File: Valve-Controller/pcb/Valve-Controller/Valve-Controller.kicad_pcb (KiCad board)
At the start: 2 copper layers, 26.9 x 26.9 mm, 14 parts, among them J1 Screw_Terminal_01x02, J2 Conn_01x03_Socket, Q1 SiS454DN

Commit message: Updated Valve Controller PCB and BOM
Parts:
- added D1: D, Diode_SMD:D_SOD-123, F.Cu at (40.8, 32.1)
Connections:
- net +3.3V renamed +12V
- net /PyroController/Input renamed /ValveController/Input
- net /PyroController/Output renamed /ValveController/Output
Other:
- board text added: "Valve Controller Rev. 1"
- board text removed: "Pyro Controller Rev. 1"

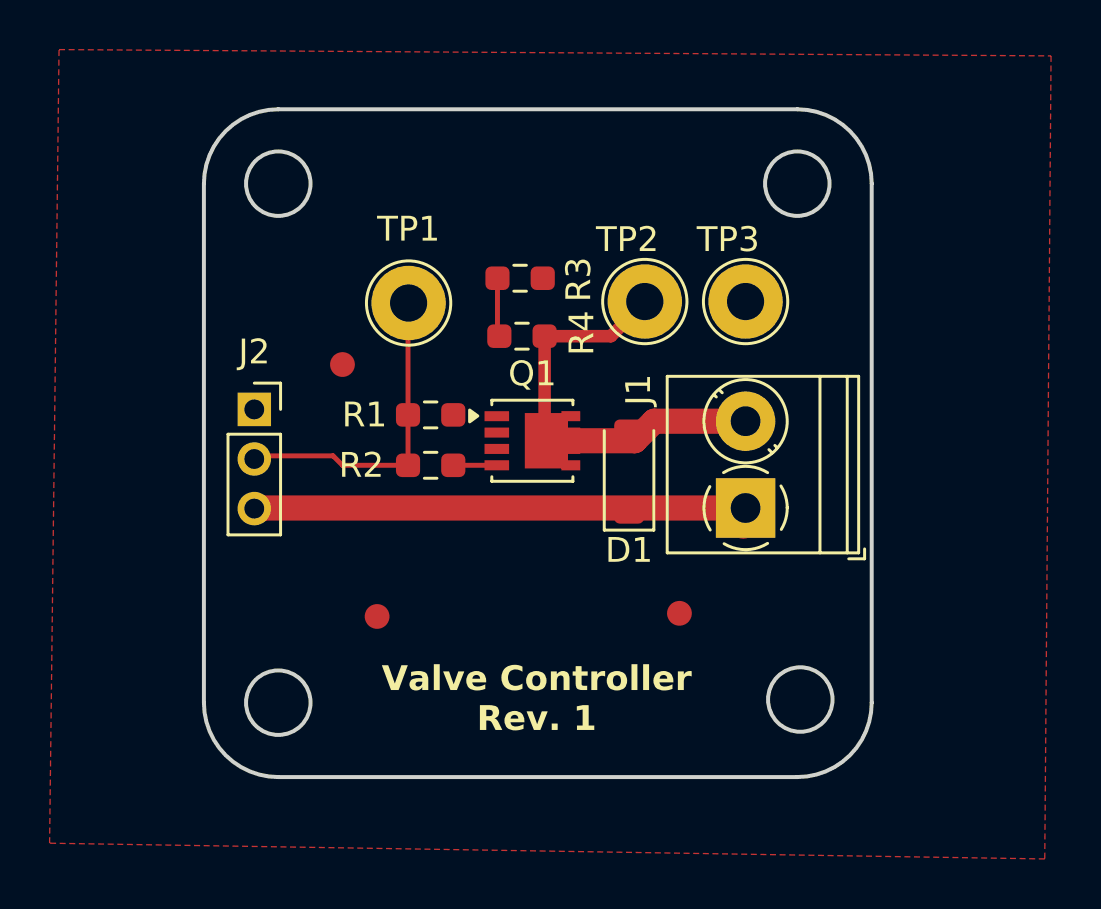
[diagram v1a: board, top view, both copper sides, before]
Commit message: Fixed valve controller pin socket. Now 2.54mm pitch
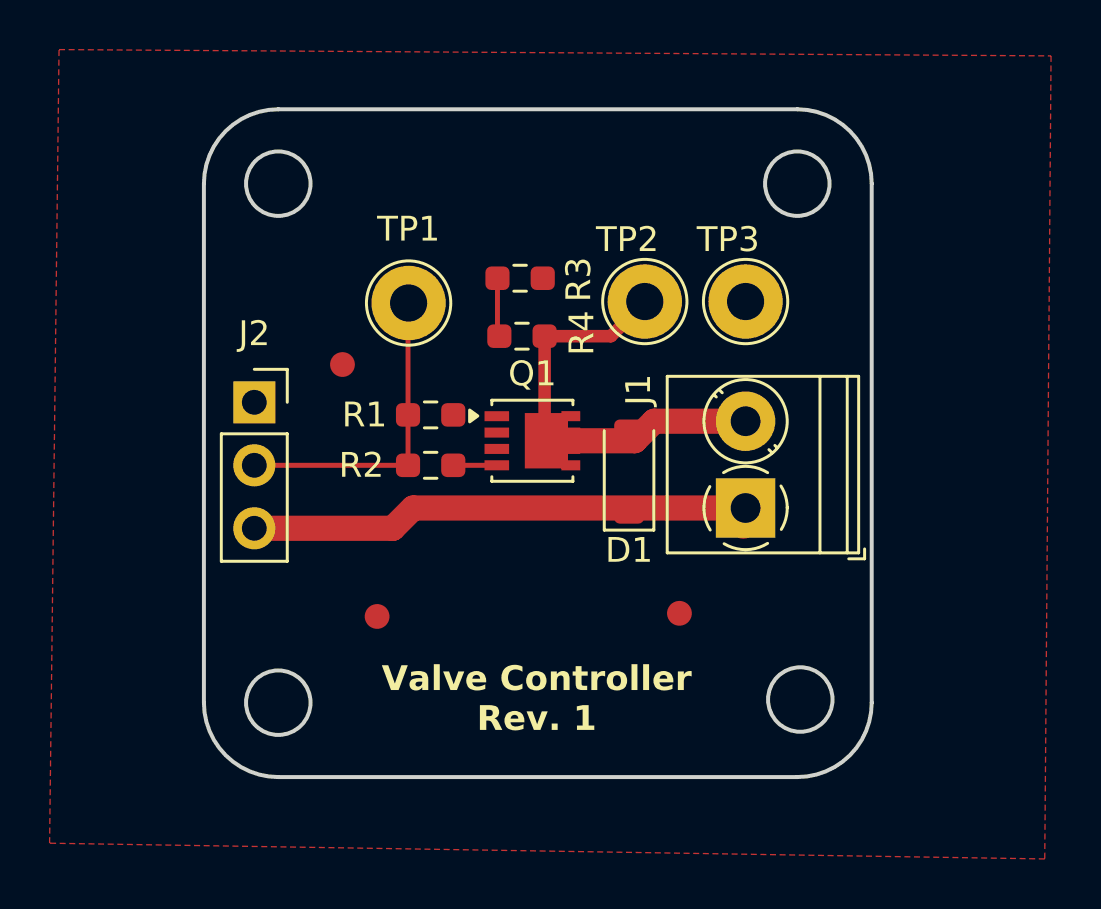
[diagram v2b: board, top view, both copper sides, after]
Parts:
- J2: footprint Connector_PinSocket_2.00mm:PinSocket_1x03_P2.00mm_Vertical -> Connector_PinSocket_2.54mm:PinSocket_1x03_P2.54mm_Vertical
- moved J2 0.29 mm to (25.7, 29.3)
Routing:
- net +12V: track 20.4 -> 20.9 mm
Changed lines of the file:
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@@
 			)
 		)
-		(property "Datasheet" ""
+		(property "Datasheet" "https://www.onsemi.com/pdf/datasheet/mmsd4148t1-d.pdf"
 			(at 0 0 90)
 			(unlocked yes)
@@
 			)
 		)
+		(property "Purchase" "https://www.digikey.com/en/products/detail/onsemi/MMSD4148T1G/919705"
+			(at 0 0 90)
+			(unlocked yes)
+			(layer "F.Fab")
+			(hide yes)
+			(effects
+				(font
+					(size 1 1)
+					(thickness 0.15)
+				)
+			)
+		)
 		(property ki_fp_filters "TO-???* *_Diode_* *SingleDiode* D_*")
 		(sheetname "ValveController")
@@
 		)
 	)
-	(footprint "Connector_PinSocket_2.00mm:PinSocket_1x03_P2.00mm_Vertical"
+	(footprint "Connector_PinSocket_2.54mm:PinSocket_1x03_P2.54mm_Vertical"
 		(layer "F.Cu")
-		(at 25.654 29.623)
-		(descr "Through hole straight socket strip, 1x03, 2.00mm pitch, single row (from Kicad 4.0.7), script generated")
-		(tags "Through hole socket strip THT 1x03 2.00mm single row")
+		(at 25.654 29.337)
+		(descr "Through hole straight socket strip, 1x03, 2.54mm pitch, single row (from Kicad 4.0.7), script generated")
+		(tags "Through hole socket strip THT 1x03 2.54mm single row")
 		(property "Reference" "J2"
-			(at 0 -2.318 0)
+			(at 0 -2.77 0)
 			(layer "F.SilkS")
 			(effects
@@
 		)
 		(property "Value" "Conn_01x03_Socket"
-			(at 0 6.5 0)
+			(at 0 7.85 0)
 			(layer "F.Fab")
 			(effects
@@
 			)
 		)
-		(property "Footprint" "Connector_PinSocket_2.00mm:PinSocket_1x03_P2.00mm_Vertical"
+		(property "Footprint" "Connector_PinSocket_2.54mm:PinSocket_1x03_P2.54mm_Vertical"
 			(at 0 0 0)
 			(unlocked yes)
@@
 		(attr through_hole)
 		(fp_line
-			(start -1.06 1)
-			(end -1.06 5.06)
+			(start -1.33 1.27)
+			(end -1.33 6.41)
 			(stroke
 				(width 0.12)
@@
 		)
 		(fp_line
-			(start -1.06 1)
-			(end 1.06 1)
+			(start -1.33 1.27)
+			(end 1.33 1.27)
 			(stroke
 				(width 0.12)
@@
 		)
 		(fp_line
-			(start -1.06 5.06)
-			(end 1.06 5.06)
+			(start -1.33 6.41)
+			(end 1.33 6.41)
 			(stroke
 				(width 0.12)
@@
 		)
 		(fp_line
-			(start 0 -1.06)
-			(end 1.06 -1.06)
+			(start 0 -1.33)
+			(end 1.33 -1.33)
 			(stroke
 				(width 0.12)
@@
 		)
 		(fp_line
-			(start 1.06 -1.06)
-			(end 1.06 0)
+			(start 1.33 -1.33)
+			(end 1.33 0)
 			(stroke
 				(width 0.12)
@@
 		)
 		(fp_line
-			(start 1.06 1)
-			(end 1.06 5.06)
+			(start 1.33 1.27)
+			(end 1.33 6.41)
 			(stroke
 				(width 0.12)
@@
 		)
 		(fp_line
-			(start -1.5 -1.5)
-			(end 1.5 -1.5)
+			(start -1.8 -1.8)
+			(end 1.75 -1.8)
 			(stroke
 				(width 0.05)
@@
 		)
 		(fp_line
-			(start -1.5 5.5)
-			(end -1.5 -1.5)
+			(start -1.8 6.85)
+			(end -1.8 -1.8)
 			(stroke
 				(width 0.05)
@@
 		)
 		(fp_line
-			(start 1.5 -1.5)
-			(end 1.5 5.5)
+			(start 1.75 -1.8)
+			(end 1.75 6.85)
 			(stroke
 				(width 0.05)
@@
 		)
 		(fp_line
-			(start 1.5 5.5)
-			(end -1.5 5.5)
+			(start 1.75 6.85)
+			(end -1.8 6.85)
 			(stroke
 				(width 0.05)
@@
 		)
 		(fp_line
-			(start -1 -1)
-			(end 0.5 -1)
+			(start -1.27 -1.27)
+			(end 0.635 -1.27)
 			(stroke
 				(width 0.1)
@@
 		)
 		(fp_line
-			(start -1 5)
-			(end -1 -1)
+			(start -1.27 6.35)
+			(end -1.27 -1.27)
 			(stroke
 				(width 0.1)
@@
 		)
 		(fp_line
-			(start 0.5 -1)
-			(end 1 -0.5)
+			(start 0.635 -1.27)
+			(end 1.27 -0.635)
 			(stroke
 				(width 0.1)
@@
 		)
 		(fp_line
-			(start 1 -0.5)
-			(end 1 5)
+			(start 1.27 -0.635)
+			(end 1.27 6.35)
 			(stroke
 				(width 0.1)
@@
 		)
 		(fp_line
-			(start 1 5)
-			(end -1 5)
+			(start 1.27 6.35)
+			(end -1.27 6.35)
 			(stroke
 				(width 0.1)
@@
 		)
 		(fp_text user "${REFERENCE}"
-			(at 0 2 90)
+			(at 0 2.54 90)
 			(layer "F.Fab")
 			(effects
@@
 		(pad "1" thru_hole rect
 			(at 0 0)
-			(size 1.35 1.35)
-			(drill 0.8)
+			(size 1.7 1.7)
+			(drill 1)
 			(layers "*.Cu" "*.Mask")
 			(remove_unused_layers no)
@@
 		)
 		(pad "2" thru_hole oval
-			(at 0 2)
-			(size 1.35 1.35)
-			(drill 0.8)
+			(at 0 2.54)
+			(size 1.7 1.7)
+			(drill 1)
 			(layers "*.Cu" "*.Mask")
 			(remove_unused_layers no)
@@
 		)
 		(pad "3" thru_hole oval
-			(at 0 4)
-			(size 1.35 1.35)
-			(drill 0.8)
+			(at 0 5.08)
+			(size 1.7 1.7)
+			(drill 1)
 			(layers "*.Cu" "*.Mask")
 			(remove_unused_layers no)
@@
 			(pintype "passive")
 		)
-		(model "${KICAD8_3DMODEL_DIR}/Connector_PinSocket_2.00mm.3dshapes/PinSocket_1x03_P2.00mm_Vertical.wrl"
+		(model "${KICAD8_3DMODEL_DIR}/Connector_PinSocket_2.54mm.3dshapes/PinSocket_1x03_P2.54mm_Vertical.wrl"
 			(offset
 				(xyz 0 0 0)
@@
 	(segment
 		(start 45.466 33.599)
-		(end 25.964 33.599)
+		(end 32.06 33.599)
 		(width 1.016)
 		(layer "F.Cu")
@@
 	)
 	(segment
-		(start 25.964 33.599)
-		(end 25.908 33.655)
+		(start 31.242 34.417)
+		(end 25.654 34.417)
+		(width 1.016)
+		(layer "F.Cu")
+		(net 1)
+	)
+	(segment
+		(start 32.06 33.599)
+		(end 31.242 34.417)
 		(width 1.016)
 		(layer "F.Cu")
@@
 	)
 	(segment
-		(start 28.829 31.496)
-		(end 25.781 31.496)
-		(width 0.2)
-		(layer "F.Cu")
-		(net 5)
-	)
-	(segment
 		(start 31.8535 31.877)
-		(end 29.21 31.877)
-		(width 0.2)
-		(layer "F.Cu")
-		(net 5)
-	)
-	(segment
-		(start 29.21 31.877)
-		(end 28.829 31.496)
+		(end 25.908 31.877)
 		(width 0.2)
 		(layer "F.Cu")
@@
 	)
 	(segment
-		(start 25.781 31.496)
+		(start 25.908 31.877)
 		(end 25.654 31.623)
 		(width 0.2)
